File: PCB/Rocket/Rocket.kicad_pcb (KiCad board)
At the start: 2 copper layers, 47 parts, among them J1 Conn_01x08_Pin, J2 Conn_01x04_Pin, J3 Conn_01x07_Pin, J4 Micro_SD_Card, J5 Conn_ARM_JTAG_SWD_10, J6 Conn_01x04_Pin, J7 1987724, SW1 CK_KMS2xxG, SW2 CK_KMS2xxG, U1 STM32L476RGTx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

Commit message: Fixing DRC errors.
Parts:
- moved CR1 6.52 mm to (136.2, 97.5)
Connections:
- U1 pad 56: /NRST -> unconnected-(U1-PB4-Pad56)
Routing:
- net GND: track 69.2 -> 61.3 mm, vias 24 -> 25
- net +3.3V: track 23.0 -> 17.2 mm
- added copper zone on B.Cu, net GND
- removed copper zone on B.Cu, net +3.3V
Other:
- board outline added: 71 x 69.5 mm

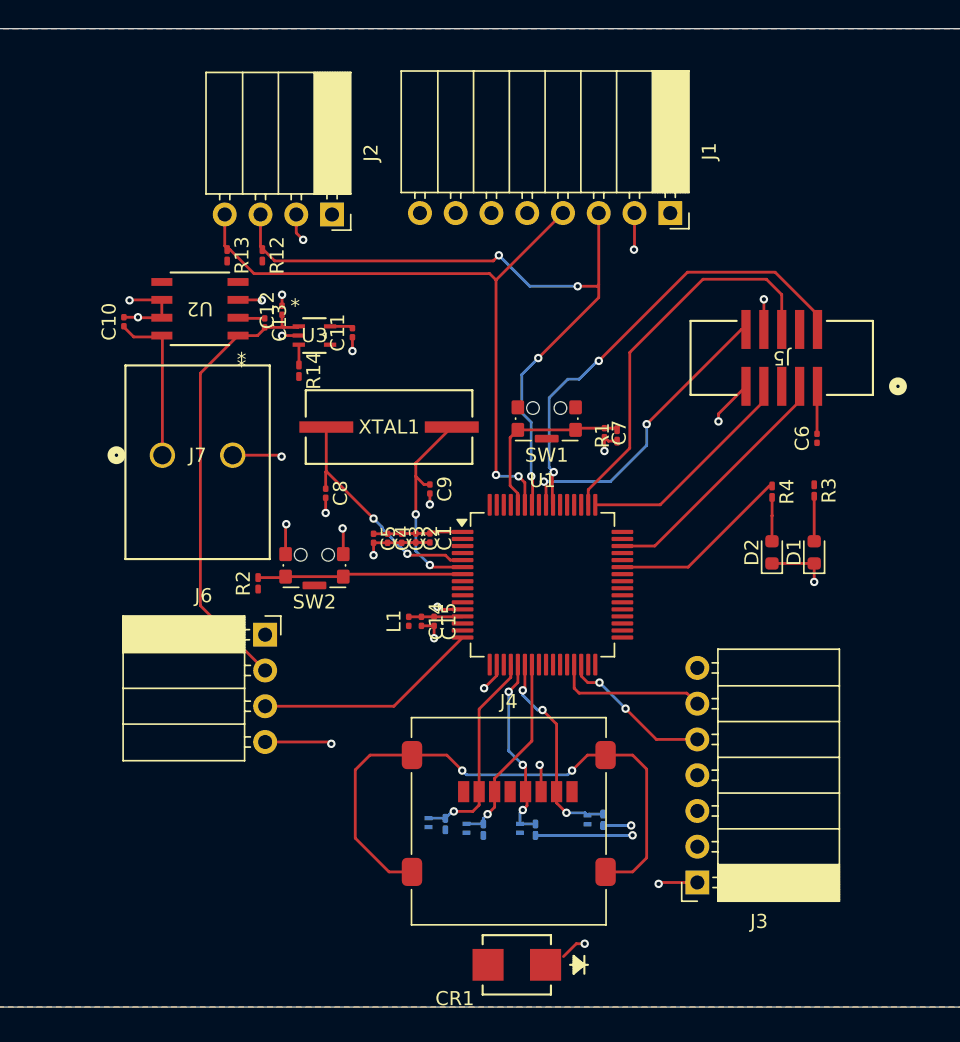
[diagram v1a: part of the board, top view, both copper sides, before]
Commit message: Removed silkscreen errors.
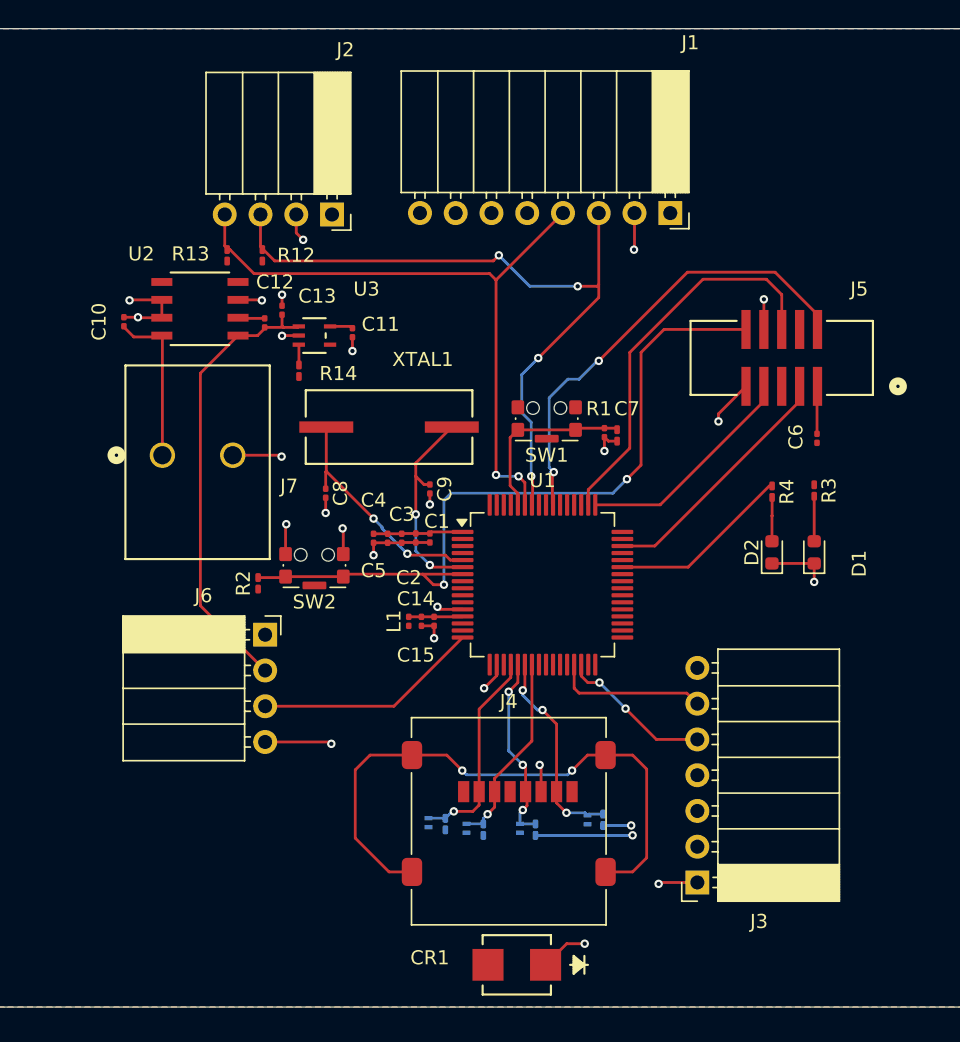
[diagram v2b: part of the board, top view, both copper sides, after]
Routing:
- net /NRST: track 36.0 -> 53.6 mm
- net GND: track 61.3 -> 62.8 mm

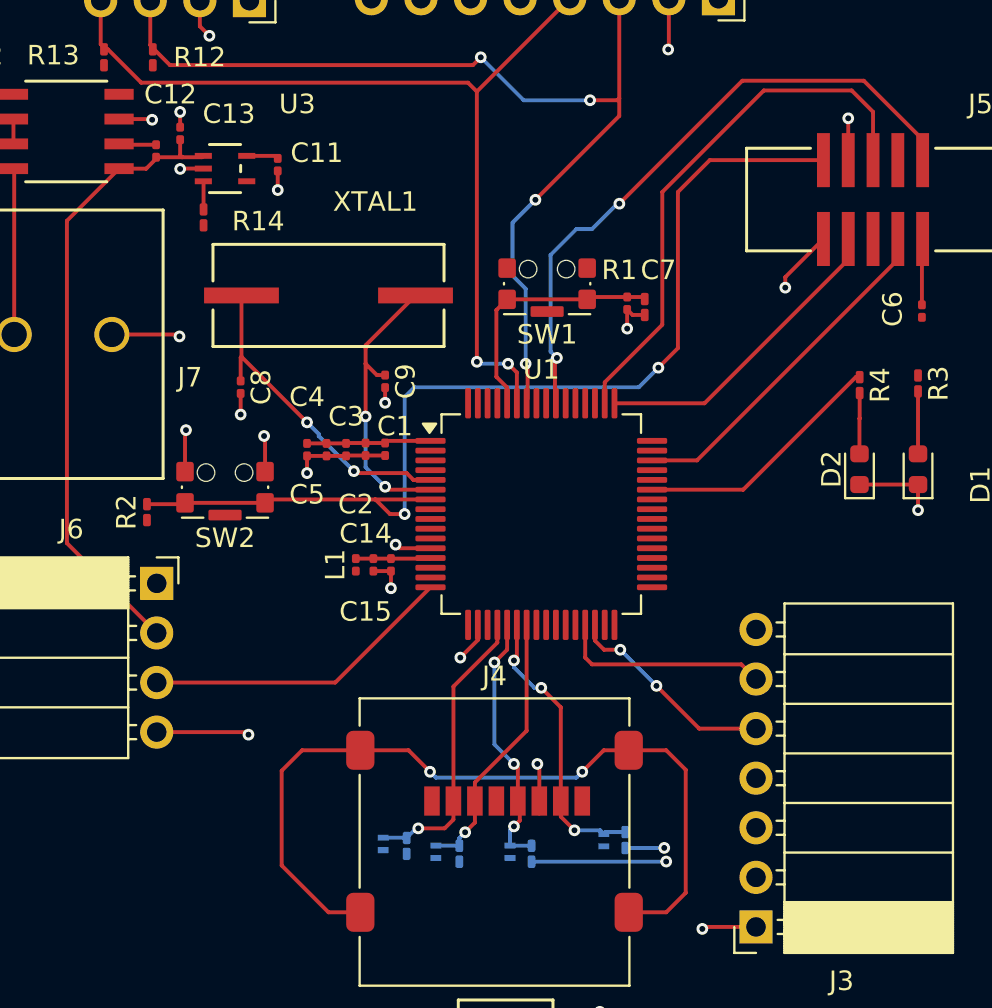
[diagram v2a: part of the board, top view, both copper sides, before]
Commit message: Removed all DRC errors.
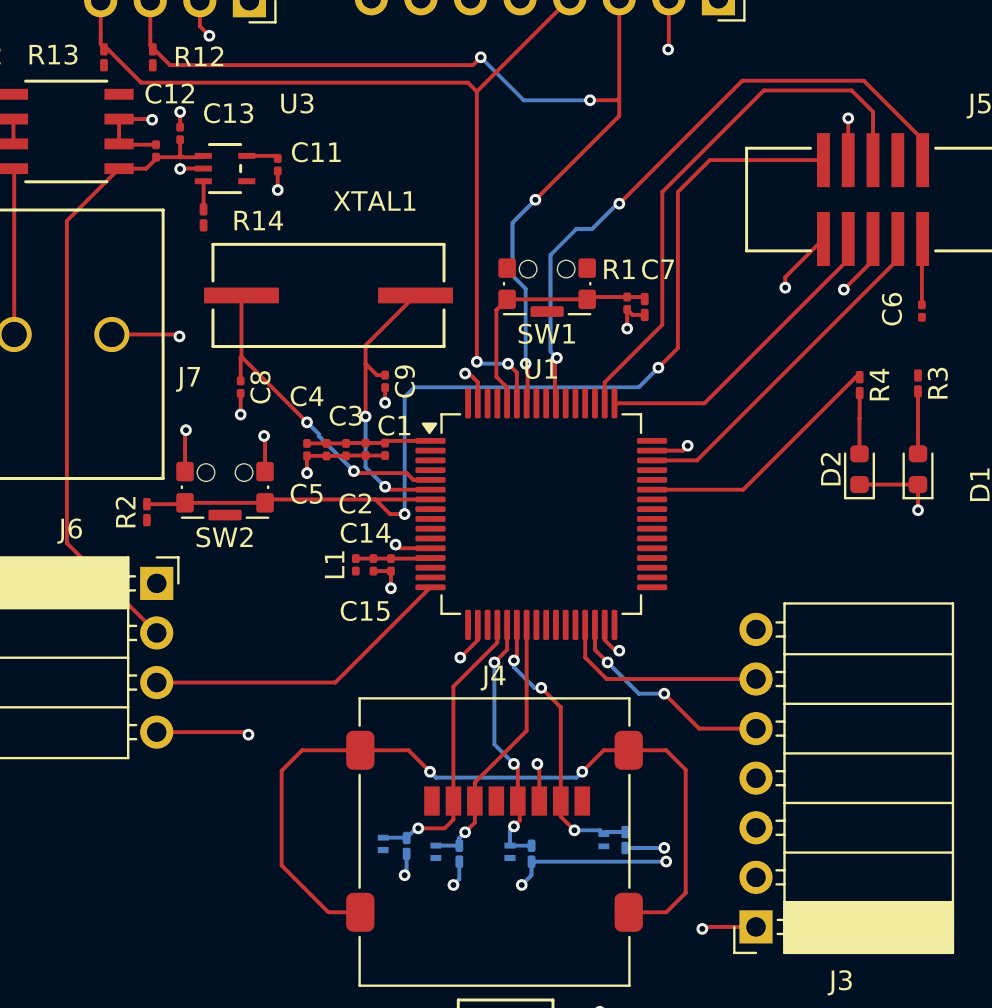
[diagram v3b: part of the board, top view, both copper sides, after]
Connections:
- C6 pad 1: +3.3VA -> +3.3V
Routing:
- net GND: track 62.8 -> 72.9 mm, vias 25 -> 29
- net +3.3V: track 17.2 -> 21.1 mm, vias 2 -> 5
- net /TX: track 10.9 -> 11.5 mm
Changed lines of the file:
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@@
 			(layers "F.Cu" "F.Mask")
 			(roundrect_rratio 0.25)
-			(net 73 "+3.3VA")
+			(net 72 "+3.3V")
 			(pintype "passive")
 		)
@@
 	)
 	(segment
-		(start 146.09 81.49)
-		(end 143.9 79.3)
+		(start 144.3 79.7)
+		(end 146.09 81.49)
 		(width 0.2)
 		(layer "F.Cu")
@@
 	)
 	(segment
-		(start 142.05 77.45)
-		(end 141.21759 77.45)
+		(start 146.09 81.49)
+		(end 149 81.49)
 		(width 0.2)
 		(layer "F.Cu")
@@
 	)
 	(segment
-		(start 141.21759 77.45)
-		(end 140.75 76.98241)
+		(start 140.75 77.45)
+		(end 141.4 78.1)
 		(width 0.2)
 		(layer "F.Cu")
@@
 	)
 	(segment
-		(start 140.75 76.98241)
-		(end 140.75 76.175)
+		(start 140.75 77.25)
+		(end 140.75 77.45)
 		(width 0.2)
 		(layer "F.Cu")
@@
 	)
 	(segment
-		(start 149 81.49)
-		(end 146.09 81.49)
+		(start 140.75 76.175)
+		(end 140.75 77.25)
 		(width 0.2)
 		(layer "F.Cu")
@@
 	)
 	(via
-		(at 143.9 79.3)
+		(at 144.3 79.7)
 		(size 0.6)
 		(drill 0.3)
@@
 	)
 	(via
-		(at 142.05 77.45)
+		(at 141.4 78.1)
 		(size 0.6)
 		(drill 0.3)
@@
 	)
 	(segment
-		(start 143.9 79.3)
-		(end 142.05 77.45)
+		(start 143 79.7)
+		(end 144.3 79.7)
 		(width 0.2)
 		(layer "B.Cu")
@@
 	)
 	(segment
-		(start 142.05 77.45)
-		(end 142 77.4)
+		(start 141.4 78.1)
+		(end 143 79.7)
 		(width 0.2)
 		(layer "B.Cu")
@@
 	)
 	(segment
-		(start 148.25 78.2)
-		(end 140.6 78.2)
+		(start 148.55 78.5)
+		(end 149 78.95)
 		(width 0.2)
 		(layer "F.Cu")
@@
 	(segment
 		(start 140.25 77.85)
-		(end 140.25 76.175)
+		(end 141.35 78.95)
 		(width 0.2)
 		(layer "F.Cu")
@@
 	)
 	(segment
-		(start 149 78.95)
-		(end 148.25 78.2)
+		(start 141.35 78.95)
+		(end 149 78.95)
 		(width 0.2)
 		(layer "F.Cu")
@@
 	)
 	(segment
-		(start 140.6 78.2)
+		(start 140.25 76.175)
 		(end 140.25 77.85)
 		(width 0.2)
@@
 	)
 	(via
+		(at 131 89)
+		(size 0.6)
+		(drill 0.3)
+		(layers "F.Cu" "B.Cu")
+		(net 72)
+	)
+	(via
+		(at 137 89.5)
+		(size 0.6)
+		(drill 0.3)
+		(layers "F.Cu" "B.Cu")
+		(net 72)
+	)
+	(via
 		(at 144.3 87.6)
 		(size 0.6)
@@
 		(net 72)
 	)
+	(via
+		(at 133.5 89.5)
+		(size 0.6)
+		(drill 0.3)
+		(layers "F.Cu" "B.Cu")
+		(net 72)
+	)
+	(segment
+		(start 133.8 89.2)
+		(end 133.5 89.5)
+		(width 0.2)
+		(layer "B.Cu")
+		(net 72)
+	)
+	(segment
+		(start 131.1 88.9)
+		(end 131 89)
+		(width 0.2)
+		(layer "B.Cu")
+		(net 72)
+	)
 	(segment
 		(start 142.3 87.6075)
@@
 	)
 	(segment
+		(start 131.1 87.9075)
+		(end 131.1 88.9)
+		(width 0.2)
+		(layer "B.Cu")
+		(net 72)
+	)
+	(segment
+		(start 137.5 89)
+		(end 137 89.5)
+		(width 0.2)
+		(layer "B.Cu")
+		(net 72)
+	)
+	(segment
 		(start 144.2925 87.6075)
 		(end 144.3 87.6)
@@
 	)
 	(segment
+		(start 133.8 88.3075)
+		(end 133.8 89.2)
+		(width 0.2)
+		(layer "B.Cu")
+		(net 72)
+	)
+	(segment
+		(start 137.5 88.3075)
+		(end 137.5 89)
+		(width 0.2)
+		(layer "B.Cu")
+		(net 72)
+	)
+	(segment
 		(start 128.5 72.78)
 		(end 129.4 72.78)
@@
 	)
 	(segment
+		(start 134.75 64.825)
+		(end 134.75 63.75)
+		(width 0.2)
+		(layer "F.Cu")
+		(net 76)
+	)
+	(segment
 		(start 109.2666 51.5)
 		(end 108.2666 51.5)
@@
 	)
 	(segment
+		(start 145.25 67.25)
+		(end 145.5 67)
+		(width 0.2)
+		(layer "F.Cu")
+		(net 76)
+	)
+	(segment
 		(start 108.7016 50.265)
 		(end 108.6666 50.3)
@@
 	)
 	(segment
+		(start 141.795876 77.5)
+		(end 141.25 76.954124)
+		(width 0.2)
+		(layer "F.Cu")
+		(net 76)
+	)
+	(segment
 		(start 118.0316 50.265)
 		(end 118.0666 50.3)
@@
 	)
 	(segment
+		(start 142 77.5)
+		(end 141.795876 77.5)
+		(width 0.2)
+		(layer "F.Cu")
+		(net 76)
+	)
+	(segment
 		(start 118.2666 51.58)
 		(end 116.4167 51.58)
@@
 	)
 	(segment
+		(start 134.3 63.3)
+		(end 134.1 63.3)
+		(width 0.2)
+		(layer "F.Cu")
+		(net 76)
+	)
+	(segment
 		(start 142.4 60.02)
 		(end 142.4 61)
@@
 	)
 	(segment
+		(start 154.9951 56.407248)
+		(end 154.9951 57.5049)
+		(width 0.2)
+		(layer "F.Cu")
+		(net 76)
+	)
+	(segment
 		(start 133.852062 77.852062)
 		(end 134.75 76.954124)
@@
 	)
 	(segment
+		(start 143.675 67.25)
+		(end 145.25 67.25)
+		(width 0.2)
+		(layer "F.Cu")
+		(net 76)
+	)
+	(segment
 		(start 130 67.5)
 		(end 129 67.5)
@@
 	)
 	(segment
+		(start 116.3717 51.535)
+		(end 116.3717 50.265)
+		(width 0.2)
+		(layer "F.Cu")
+		(net 76)
+	)
+	(segment
 		(start 139.7192 96)
 		(end 141 96)
@@
 	)
 	(segment
+		(start 134.5 63.5)
+		(end 134.3 63.3)
+		(width 0.2)
+		(layer "F.Cu")
+		(net 76)
+	)
+	(segment
 		(start 154.3 68.9875)
 		(end 157.3 68.9875)
@@
 	)
 	(segment
+		(start 141.25 76.954124)
+		(end 141.25 76.175)
+		(width 0.2)
+		(layer "F.Cu")
+		(net 76)
+	)
+	(segment
 		(start 123.85 68.325)
 		(end 123.85 66.55)
@@
 	)
 	(segment
+		(start 134.75 63.75)
+		(end 134.5 63.5)
+		(width 0.2)
+		(layer "F.Cu")
+		(net 76)
+	)
+	(segment
+		(start 154.9951 57.5049)
+		(end 153.5 59)
+		(width 0.2)
+		(layer "F.Cu")
+		(net 76)
+	)
+	(segment
 		(start 110.9615 51.535)
 		(end 109.3016 51.535)
@@
 	)
 	(via
+		(at 153.5 59)
+		(size 0.6)
+		(drill 0.3)
+		(layers "F.Cu" "B.Cu")
+		(net 76)
+	)
+	(via
 		(at 119.5 52.82)
 		(size 0.6)
@@
 	)
 	(via
+		(at 145.5 67)
+		(size 0.6)
+		(drill 0.3)
+		(layers "F.Cu" "B.Cu")
+		(net 76)
+	)
+	(via
+		(at 142 77.5)
+		(size 0.6)
+		(drill 0.3)
+		(layers "F.Cu" "B.Cu")
+		(net 76)
+	)
+	(via
 		(at 119.5 49.9)
 		(size 0.6)
@@
 	)
 	(via
+		(at 134.1 63.3)
+		(size 0.6)
+		(drill 0.3)
+		(layers "F.Cu" "B.Cu")
+		(net 76)
+	)
+	(via
 		(at 124.5 53.9)
 		(size 0.6)
@@
 		(hatch edge 0.5)
 		(connect_pads
-			(clearance 0.5)
+			(clearance 0.2)
 		)
 		(min_thickness 0.25)
@@
 		(priority 1)
 		(connect_pads
-			(clearance 0.5)
+			(clearance 0.2)
 		)
 		(min_thickness 0.25)
